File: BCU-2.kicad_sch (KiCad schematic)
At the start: 14 parts, among them J2 Conn_01x12_Male, J6 Conn_01x04_Male, U1 PCF8574

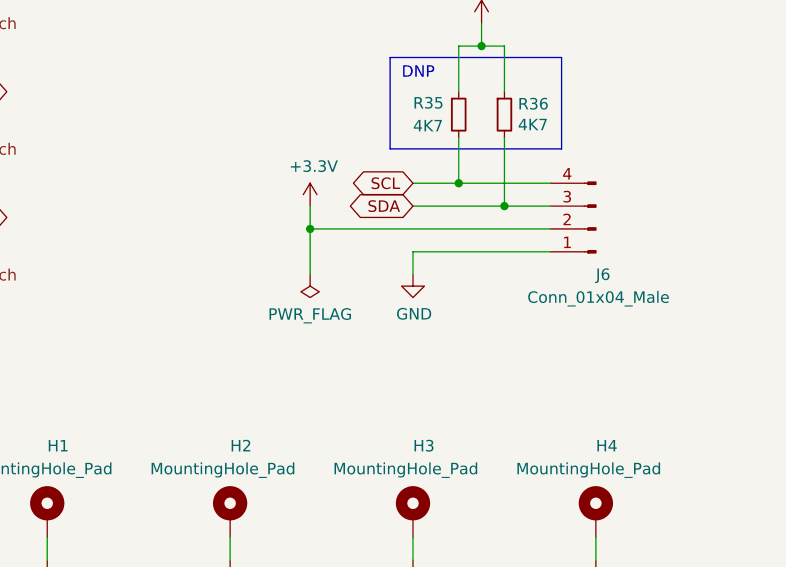
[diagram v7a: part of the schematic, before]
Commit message: Schematic: Add missing PWR_FLAG for GND
As flagged by perform electrical rules check.

Signed-off-by: Geert Uytterhoeven <geert@linux-m68k.org>
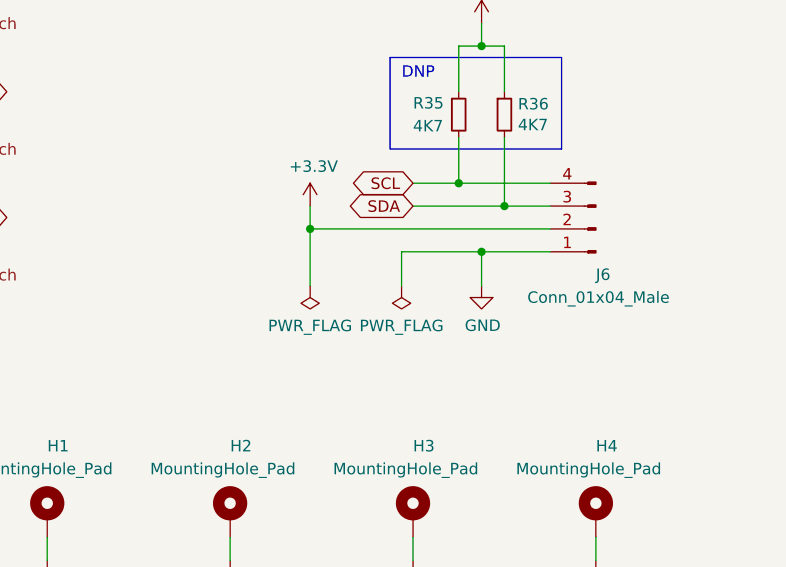
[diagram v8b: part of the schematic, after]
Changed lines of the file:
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@@
 (kicad_sch (version 20211123) (generator eeschema)
   (paper "A4")
+  (junction (at 243.84 110.49) (diameter 0) (color 0 0 0 0)
+  )
   (junction (at 99.06 137.16) (diameter 0) (color 0 0 0 0)
   )
@@
     (stroke (width 0) (type default) (color 0 0 0 0))
   )
-  (wire (pts (xy 251.46 110.49) (xy 236.22 110.49))
-    (stroke (width 0) (type default) (color 0 0 0 0))
-  )
   (wire (pts (xy 67.31 77.47) (xy 67.31 59.69))
     (stroke (width 0) (type default) (color 0 0 0 0))
@@
     (stroke (width 0) (type default) (color 0 0 0 0))
   )
-  (wire (pts (xy 236.22 110.49) (xy 236.22 113.03))
-    (stroke (width 0) (type default) (color 0 0 0 0))
-  )
   (wire (pts (xy 105.41 124.46) (xy 105.41 132.08))
     (stroke (width 0) (type default) (color 0 0 0 0))
@@
     (stroke (width 0) (type default) (color 0 0 0 0))
   )
+  (wire (pts (xy 243.84 110.49) (xy 234.95 110.49))
+    (stroke (width 0) (type default) (color 0 0 0 0))
+  )
   (wire (pts (xy 246.38 92.71) (xy 246.38 87.63))
     (stroke (width 0) (type default) (color 0 0 0 0))
@@
     (stroke (width 0) (type default) (color 0 0 0 0))
   )
-  (wire (pts (xy 224.79 107.95) (xy 224.79 113.03))
+  (wire (pts (xy 224.79 107.95) (xy 224.79 114.3))
     (stroke (width 0) (type default) (color 0 0 0 0))
   )
@@
     (stroke (width 0) (type default) (color 0 0 0 0))
   )
+  (wire (pts (xy 243.84 110.49) (xy 243.84 114.3))
+    (stroke (width 0) (type default) (color 0 0 0 0))
+  )
   (wire (pts (xy 114.3 74.93) (xy 111.76 74.93))
     (stroke (width 0) (type default) (color 0 0 0 0))
@@
     (stroke (width 0) (type default) (color 0 0 0 0))
   )
+  (wire (pts (xy 234.95 110.49) (xy 234.95 114.3))
+    (stroke (width 0) (type default) (color 0 0 0 0))
+  )
   (wire (pts (xy 99.06 137.16) (xy 101.6 137.16))
     (stroke (width 0) (type default) (color 0 0 0 0))
@@
   )
   (wire (pts (xy 165.1 93.98) (xy 167.64 93.98))
+    (stroke (width 0) (type default) (color 0 0 0 0))
+  )
+  (wire (pts (xy 251.46 110.49) (xy 243.84 110.49))
     (stroke (width 0) (type default) (color 0 0 0 0))
   )
@@
     (pin "1")
   )
-  (symbol (lib_id "power:PWR_FLAG") (at 224.79 113.03 180) (unit 1)
-    (in_bom yes) (on_board yes)
-    (property "Reference" "#FLG0101" (id 0) (at 224.79 114.935 0)
-      (effects (font (size 1.27 1.27)) hide)
-    )
-    (property "Value" "PWR_FLAG" (id 1) (at 224.79 117.4496 0))
-    (property "Footprint" "" (id 2) (at 224.79 113.03 0)
-      (effects (font (size 1.27 1.27)) hide)
-    )
-    (property "Datasheet" "~" (id 3) (at 224.79 113.03 0)
+  (symbol (lib_id "power:PWR_FLAG") (at 224.79 114.3 180) (unit 1)
+    (in_bom yes) (on_board yes)
+    (property "Reference" "#FLG0101" (id 0) (at 224.79 116.205 0)
+      (effects (font (size 1.27 1.27)) hide)
+    )
+    (property "Value" "PWR_FLAG" (id 1) (at 224.79 118.7196 0))
+    (property "Footprint" "" (id 2) (at 224.79 114.3 0)
+      (effects (font (size 1.27 1.27)) hide)
+    )
+    (property "Datasheet" "~" (id 3) (at 224.79 114.3 0)
       (effects (font (size 1.27 1.27)) hide)
     )
@@
     (pin "4")
   )
-  (symbol (lib_id "power:GND") (at 236.22 113.03 0) (unit 1)
-    (in_bom yes) (on_board yes)
-    (property "Reference" "#PWR024" (id 0) (at 236.22 119.38 0)
-      (effects (font (size 1.27 1.27)) hide)
-    )
-    (property "Value" "GND" (id 1) (at 236.347 117.4242 0))
-    (property "Footprint" "" (id 2) (at 236.22 113.03 0)
-      (effects (font (size 1.27 1.27)) hide)
-    )
-    (property "Datasheet" "" (id 3) (at 236.22 113.03 0)
+  (symbol (lib_id "power:GND") (at 243.84 114.3 0) (unit 1)
+    (in_bom yes) (on_board yes)
+    (property "Reference" "#PWR024" (id 0) (at 243.84 120.65 0)
+      (effects (font (size 1.27 1.27)) hide)
+    )
+    (property "Value" "GND" (id 1) (at 243.967 118.6942 0))
+    (property "Footprint" "" (id 2) (at 243.84 114.3 0)
+      (effects (font (size 1.27 1.27)) hide)
+    )
+    (property "Datasheet" "" (id 3) (at 243.84 114.3 0)
       (effects (font (size 1.27 1.27)) hide)
     )
@@
     )
     (property "Datasheet" "" (id 3) (at 60.96 57.15 0)
+      (effects (font (size 1.27 1.27)) hide)
+    )
+    (pin "1")
+  )
+  (symbol (lib_id "power:PWR_FLAG") (at 234.95 114.3 180) (unit 1)
+    (in_bom yes) (on_board yes)
+    (property "Reference" "#FLG?" (id 0) (at 234.95 116.205 0)
+      (effects (font (size 1.27 1.27)) hide)
+    )
+    (property "Value" "PWR_FLAG" (id 1) (at 234.95 118.7196 0))
+    (property "Footprint" "" (id 2) (at 234.95 114.3 0)
+      (effects (font (size 1.27 1.27)) hide)
+    )
+    (property "Datasheet" "~" (id 3) (at 234.95 114.3 0)
       (effects (font (size 1.27 1.27)) hide)
     )
@@
       (reference "#FLG0101") (unit 1) (value "PWR_FLAG") (footprint "")
     )
+    (path "/b7fb87a8-969f-476d-a14b-24a7d920ceee"
+      (reference "#FLG?") (unit 1) (value "PWR_FLAG") (footprint "")
+    )
     (path "/b101e671-1882-4363-b7e6-51d4d4c68639"
